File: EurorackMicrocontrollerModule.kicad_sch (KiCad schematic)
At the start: 47 parts, among them J1 Teensy4.0_Pins_Right, J2 Teensy4.0_Pins_Left, J3 Conn_01x24_Male, J4 Conn_02x05_Counter_Clockwise, J5 AudioJack, U1 PCM1754DBQ, U2 PCM1808PW, U3 AZ1117H2-ADJ

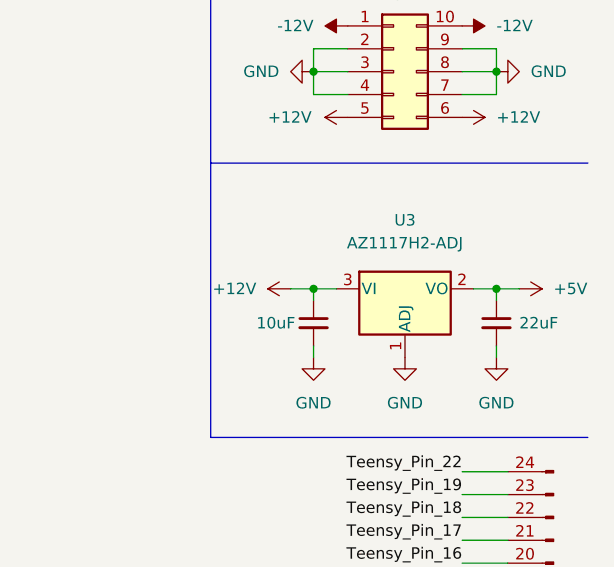
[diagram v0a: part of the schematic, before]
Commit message: Changed LDO pad layout to a more common one
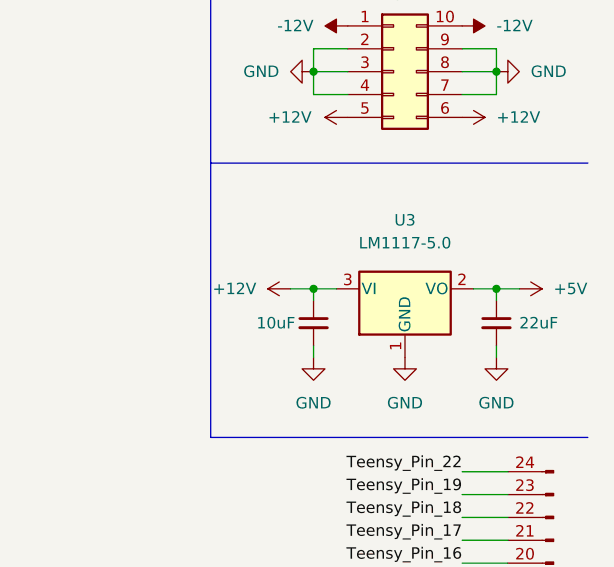
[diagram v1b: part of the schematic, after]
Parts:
- U3: value AZ1117H2-ADJ -> LM1117-5.0; symbol Regulator_Linear:AZ1117H-ADJ -> Regulator_Linear:LM1117-5.0
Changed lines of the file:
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@@
     (pin "2")
   )
-  (symbol (lib_id "Regulator_Linear:AZ1117H-ADJ") (at 264.16 48.26 0) (unit 1)
+  (symbol (lib_id "Regulator_Linear:LM1117-5.0") (at 264.16 48.26 0) (unit 1)
     (in_bom yes) (on_board yes) (fields_autoplaced)
     (property "Reference" "U3" (id 0) (at 264.16 40.64 0))
-    (property "Value" "AZ1117H2-ADJ" (id 1) (at 264.16 43.18 0))
-    (property "Footprint" "Package_TO_SOT_SMD:SOT-223-3_TabPin2" (id 2) (at 264.16 41.91 0)
-      (effects (font (size 1.27 1.27) italic) hide)
-    )
-    (property "Datasheet" "https://www.diodes.com/assets/Datasheets/products_inactive_data/AZ1117.pdf" (id 3) (at 264.16 48.26 0)
+    (property "Value" "LM1117-5.0" (id 1) (at 264.16 43.18 0))
+    (property "Footprint" "Package_TO_SOT_SMD:SOT-223-3_TabPin2" (id 2) (at 264.16 48.26 0)
+      (effects (font (size 1.27 1.27)) hide)
+    )
+    (property "Datasheet" "http://www.ti.com/lit/ds/symlink/lm1117.pdf" (id 3) (at 264.16 48.26 0)
       (effects (font (size 1.27 1.27)) hide)
     )
@@
     )
     (path "/8aa235d3-9a53-427f-8c2a-87d0e8d9e4e4"
-      (reference "U3") (unit 1) (value "AZ1117H2-ADJ") (footprint "Package_TO_SOT_SMD:SOT-223-3_TabPin2")
-    )
-  )
+      (reference "U3") (unit 1) (value "LM1117-5.0") (footprint "Package_TO_SOT_SMD:SOT-223-3_TabPin2")
+    )
+  )
